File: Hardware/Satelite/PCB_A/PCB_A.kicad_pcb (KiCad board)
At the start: 2 copper layers, 54 x 54 mm, 41 parts, among them J1 Batería LiPo (Soldada), J2 CONUFL001-SMD, J3 Servo Globo, J4 Conector_PCB_A-B, J5 Servo Paracaídas, Q1 SSM3J338R,LF, U1 A2235-H, U2 CC1101RGP, U3 0915BM15A0001E, Y1 26 MHz

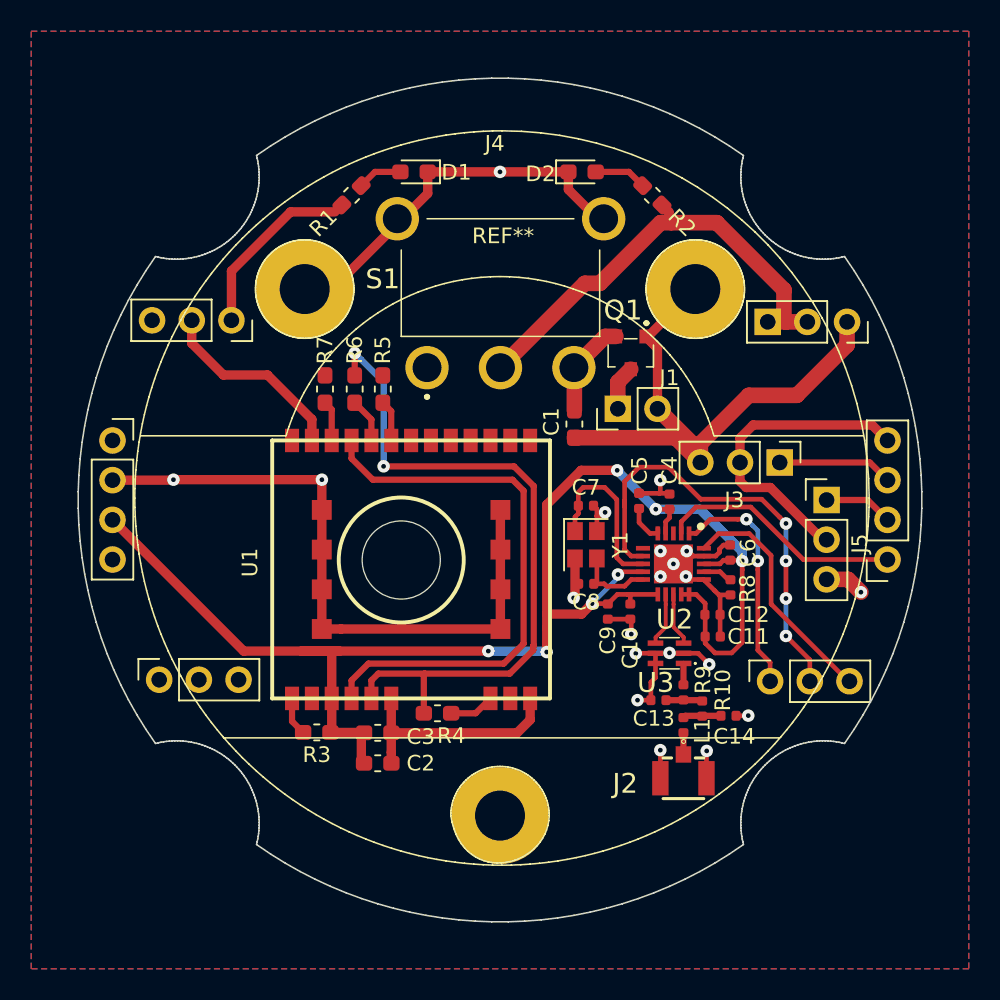
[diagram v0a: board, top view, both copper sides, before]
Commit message: Correciones de anchos de trazas en PCB A
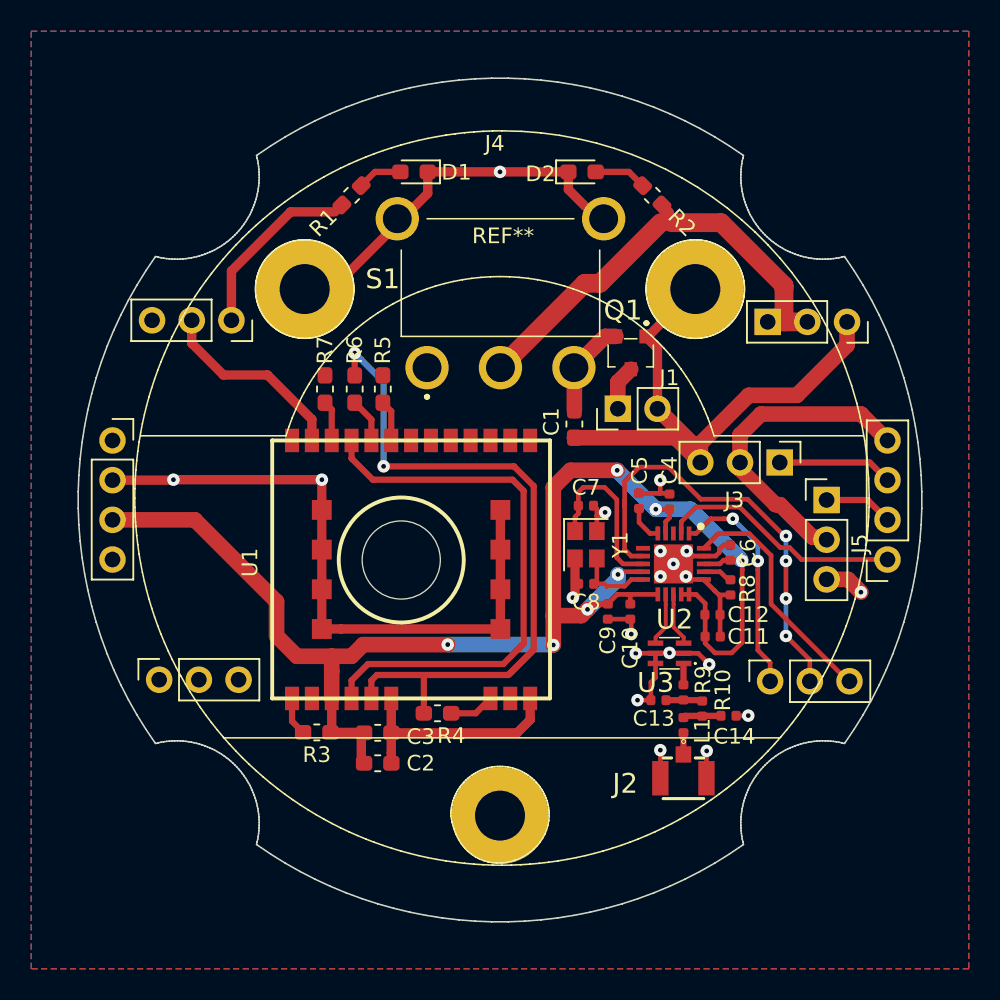
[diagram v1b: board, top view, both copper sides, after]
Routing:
- net /GPS/GPS_1V8: track 45.1 -> 47.0 mm
- net +3V3_Internal: track 98.9 -> 97.9 mm

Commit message: Numeros de parte para PCB_A. Se movió también el switch de encendido más afuera para fácil acceso.
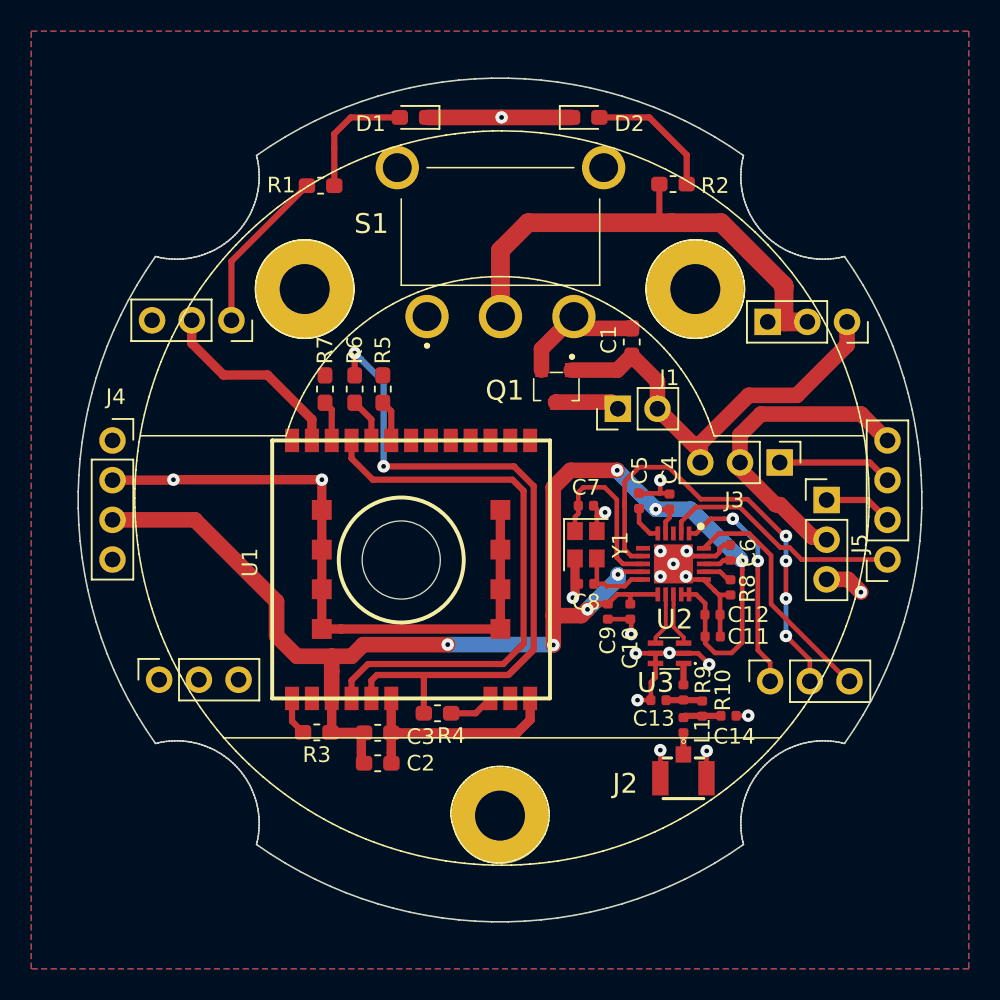
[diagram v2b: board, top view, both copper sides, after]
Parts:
- moved C1 6.41 mm to (8.43, -10.1)
- moved Q1 5.23 mm to (3.61, -7.26)
- moved D2 3.49 mm to (5.49, -24.5)
- moved D1 3.49 mm to (-5.54, -24.5)
- moved S1 3.27 mm to (0.03, -17.9)
- moved R1 2.07 mm to (-11.5, -20.1), turned to 0 degrees
- moved R2 1.51 mm to (11.1, -20.2), turned to 0 degrees
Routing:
- net GND: track 154.8 -> 130.1 mm
- net Net-(D2-Pad2): track 3.37 -> 8.45 mm
- net Net-(D1-Pad2): track 2.87 -> 7.94 mm
- net Net-(J4-Pad1): track 30.2 -> 32.6 mm
- net +BATT: track 6.85 -> 8.30 mm
- net /P1: track 12.0 -> 10.6 mm
- net Net-(J1-Pad1): track 2.87 -> 4.17 mm

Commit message: Agregados espaciadores a PCB_A
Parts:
- added M1: Spacer, AXTEC:Empty_Footprint, F.Cu at (-22.4, -24.0)
- added M2: Spacer, AXTEC:Empty_Footprint, F.Cu at (-21.9, -24.0)
- added M3: Spacer, AXTEC:Empty_Footprint, F.Cu at (-22.9, -24.0)
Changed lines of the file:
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@@
     (tracks 346)
     (zones 0)
-    (modules 41)
+    (modules 44)
     (nets 53)
   )
@@
     (add_net /CC1101/RF_P)
   )
-  (module AXTEC:PCB_mayor_diametro (layer F.Cu)
+  (module AXTEC:Empty_Footprint (layer F.Cu)
+    (at -21.9148 -23.9816)
+    (fp_text reference M2 (at 0 0.5) (layer F.SilkS) hide
+      (effects (font (size 1 1) (thickness 0.15)))
+    )
+    (fp_text value Spacer (at 0 -0.5) (layer F.Fab) hide
+      (effects (font (size 1 1) (thickness 0.15)))
+    )
+  )
+  (module AXTEC:Empty_Footprint (layer F.Cu)
+    (at -22.4148 -23.9816)
+    (fp_text reference M1 (at 0 0.5) (layer F.SilkS) hide
+      (effects (font (size 1 1) (thickness 0.15)))
+    )
+    (fp_text value Spacer (at 0 -0.5) (layer F.Fab) hide
+      (effects (font (size 1 1) (thickness 0.15)))
+    )
+  )
+  (module AXTEC:Empty_Footprint (layer F.Cu)
+    (at -22.9148 -23.9816)
+    (fp_text reference M3 (at 0 0.5) (layer F.SilkS) hide
+      (effects (font (size 1 1) (thickness 0.15)))
+    )
+    (fp_text value Spacer (at 0 -0.5) (layer F.Fab) hide
+      (effects (font (size 1 1) (thickness 0.15)))
+    )
+  )
+  (module AXTEC:PCB_mayor_diametro locked (layer F.Cu)
     (at 0 0)
     (fp_text reference REF** (at 0.2 -16.9) (layer F.SilkS) hide

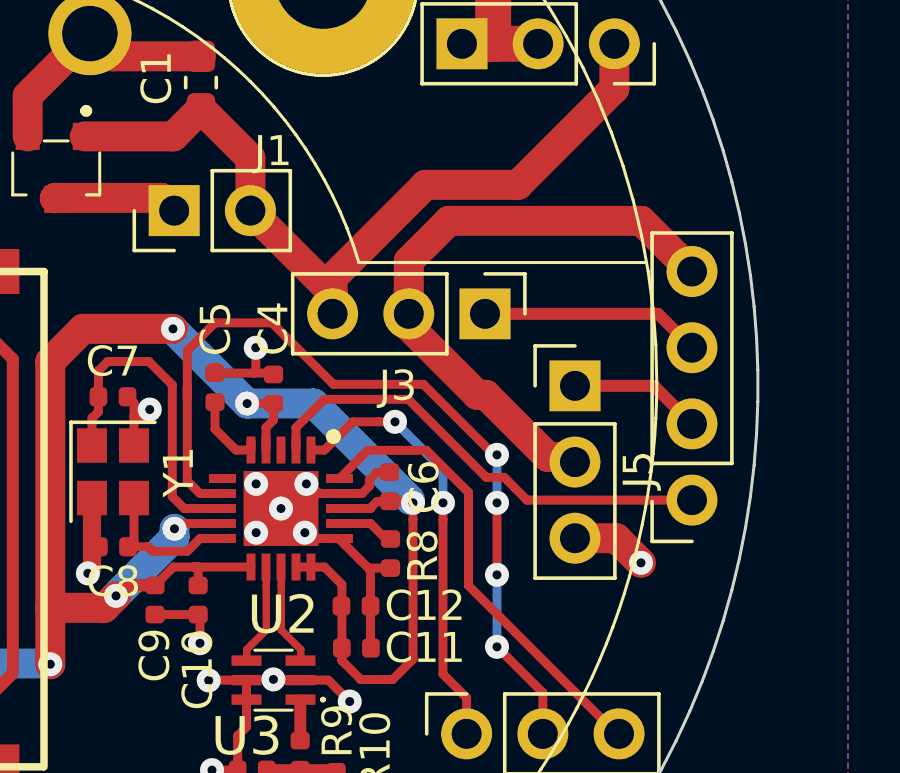
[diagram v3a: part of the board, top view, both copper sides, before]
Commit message: Indicador de conectores de servo en PCB_A
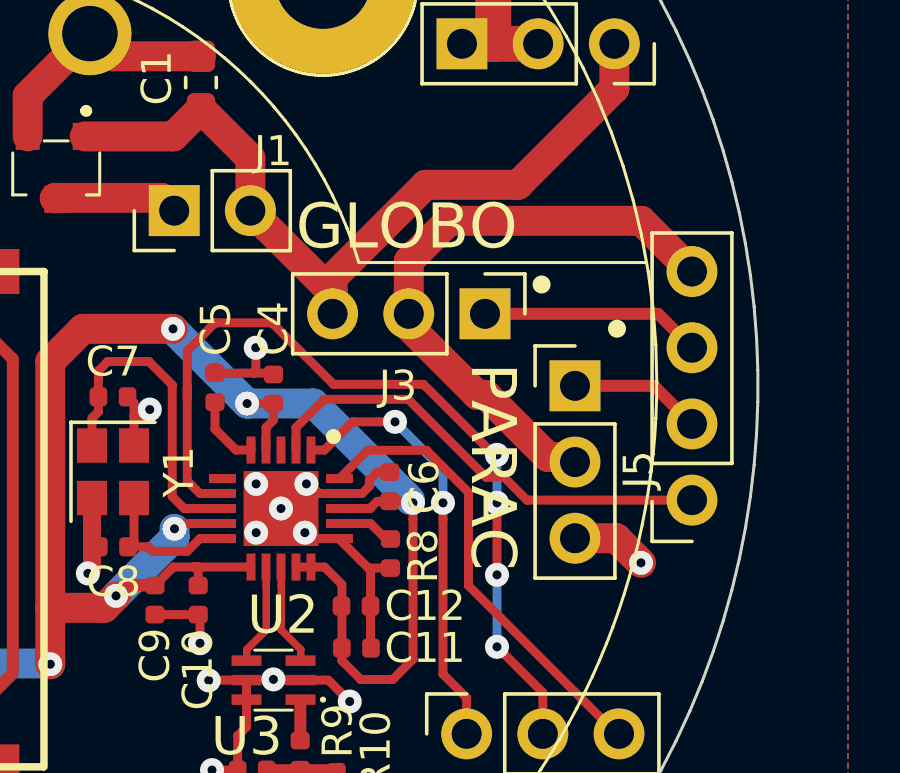
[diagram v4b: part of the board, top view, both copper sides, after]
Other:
- board text added: "GLOBO"
- board text added: "PARAC"
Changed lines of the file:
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@@
   (general
     (thickness 1.6)
-    (drawings 0)
+    (drawings 4)
     (tracks 346)
     (zones 0)
@@
     (zone_45_only no)
     (trace_min 0.2)
-    (segment_width 0.2)
+    (segment_width 0.3)
     (edge_width 0.15)
     (via_size 0.8)
@@
       (net 7 /S_GLOBO))
   )
+  (gr_circle (center 19.7866 -3.3782) (end 19.9366 -3.3782) (layer F.SilkS) (width 0.3))
+  (gr_circle (center 22.3012 -1.905) (end 22.4512 -1.905) (layer F.SilkS) (width 0.3))
+  (gr_text PARAC (at 18.161 2.6924 270) (layer F.SilkS)
+    (effects (font (size 1.5 1.5) (thickness 0.3)))
+  )
+  (gr_text GLOBO (at 15.2908 -5.3086) (layer F.SilkS)
+    (effects (font (size 1.5 1.5) (thickness 0.3)))
+  )
   (via (at 11.1 4.09) (size 0.8) (drill 0.3) (layers F.Cu B.Cu) (net 1))

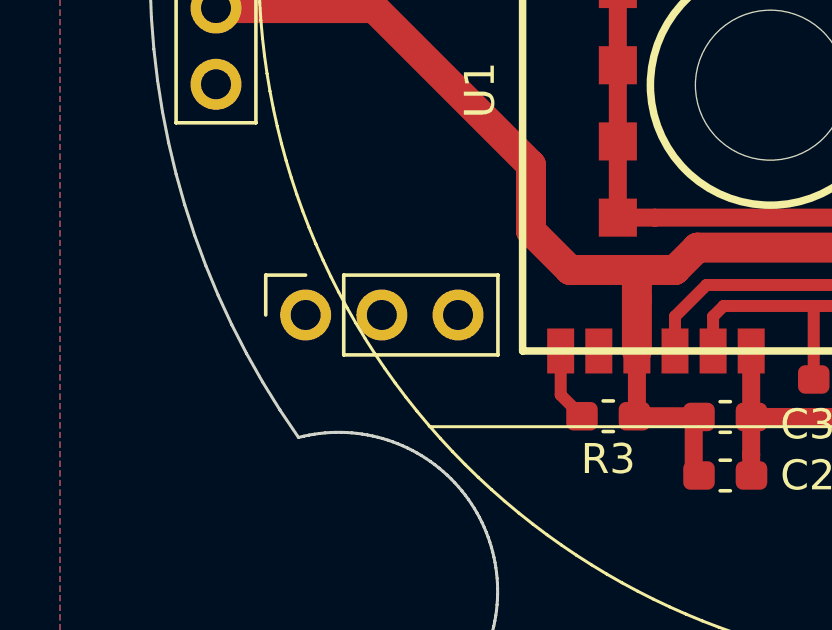
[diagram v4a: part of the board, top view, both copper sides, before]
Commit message: Eliminados pines no usados del conector A-B
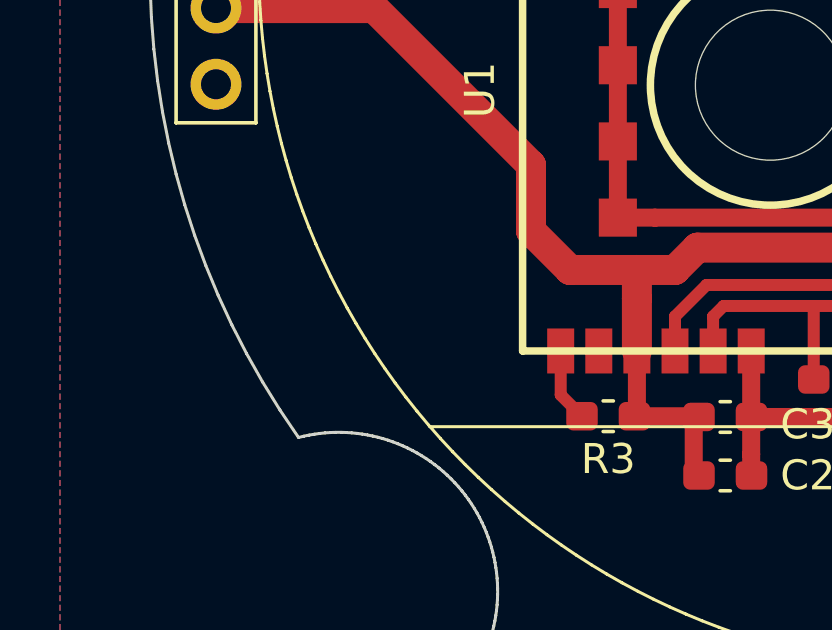
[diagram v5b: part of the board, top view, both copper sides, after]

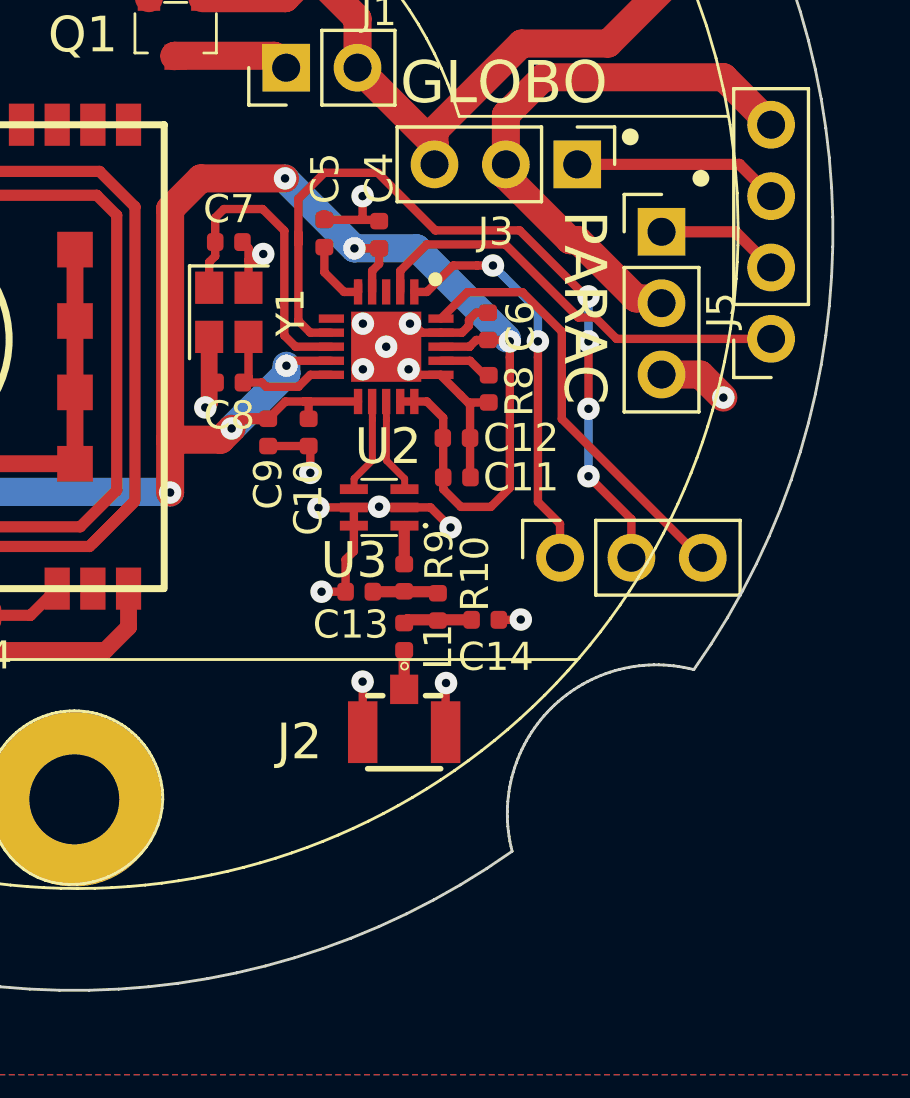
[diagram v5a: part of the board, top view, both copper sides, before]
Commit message: Modificado conector A-B para poder alojar la batería entre A y B
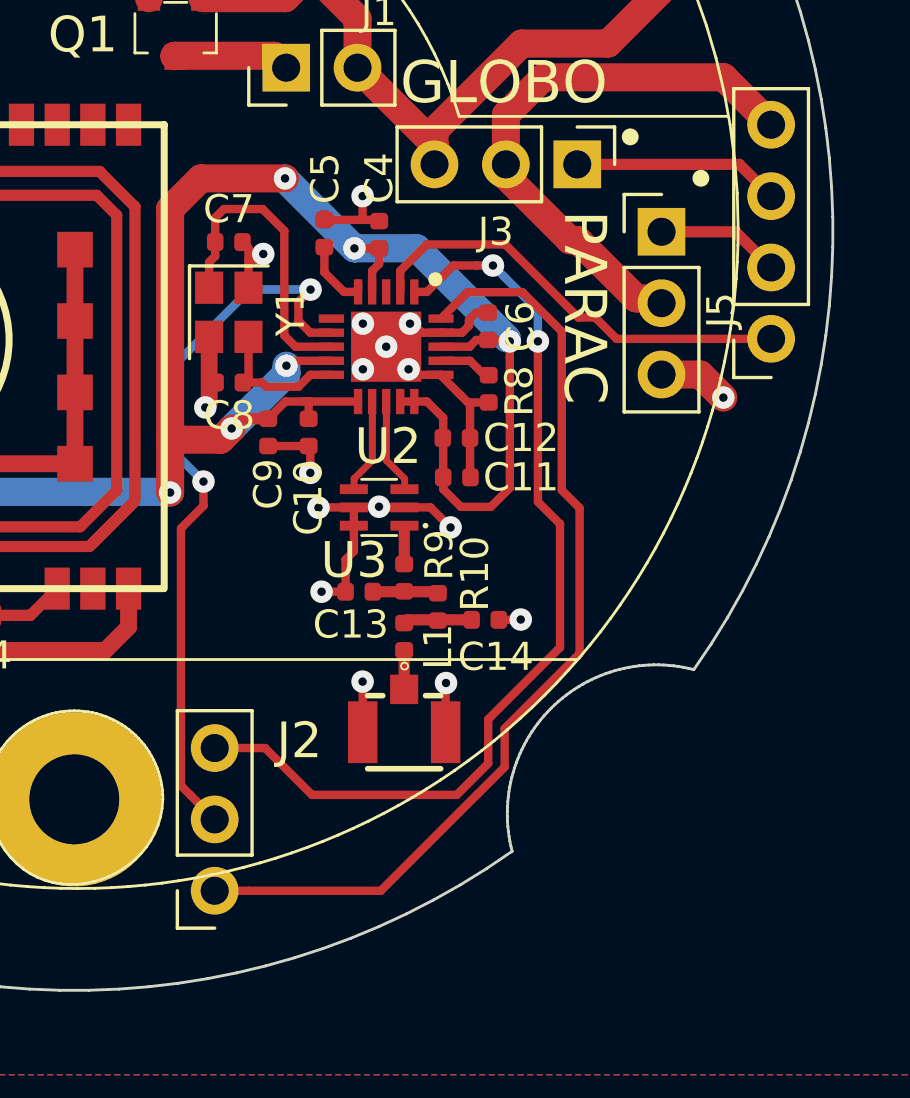
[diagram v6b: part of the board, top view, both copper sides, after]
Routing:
- net /SCLK: track 14.6 -> 33.8 mm
- net /SDI: track 15.6 -> 34.3 mm
- net /CS: track 28.5 -> 26.1 mm, vias 4 -> 2
